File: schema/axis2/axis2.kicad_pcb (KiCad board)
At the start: 2 copper layers, 69 x 110 mm, 19 parts, among them J1 JA, J2 JB, J3 5VPower, J4 12VPower, J5 Power Motor 1, J6 Power Motor 2, J7 M1, J8 M2, J9 RC-PPM, Q1 BC547, U1 gy-9250, U2 L7805, U3 axis2-frame

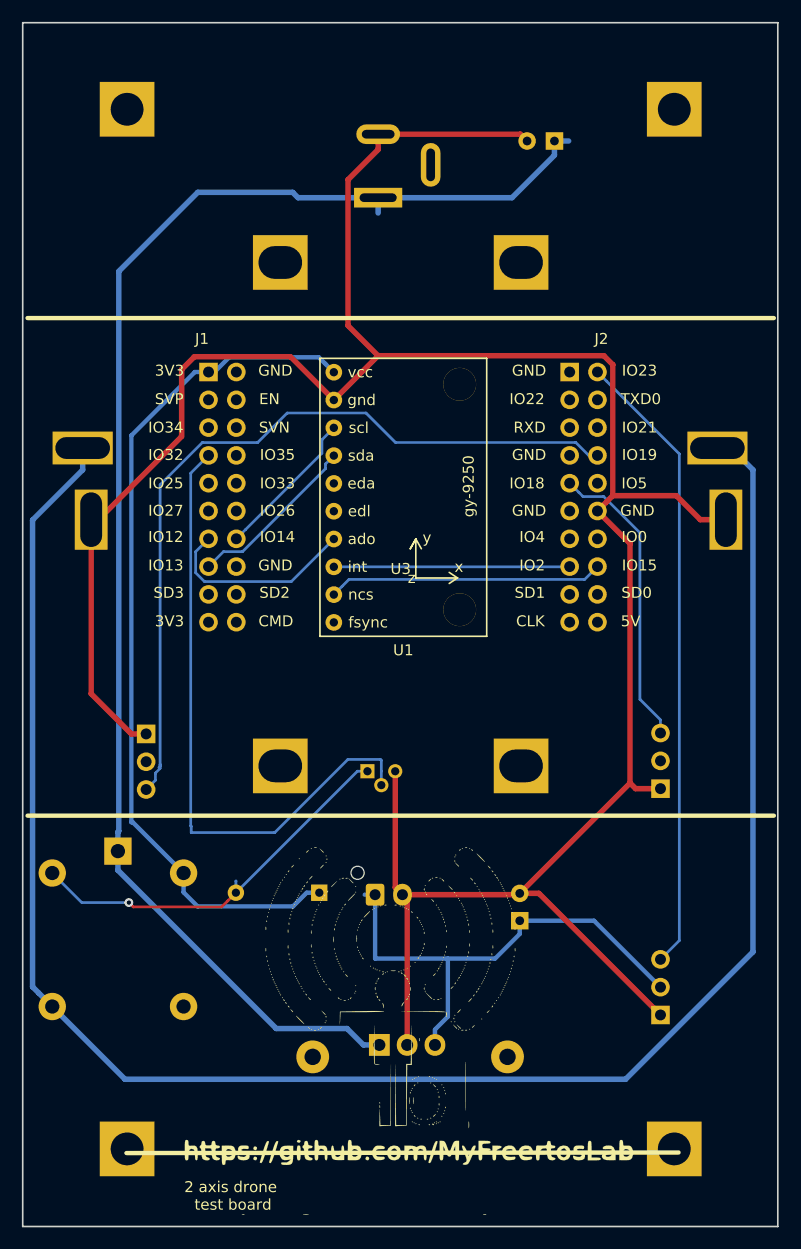
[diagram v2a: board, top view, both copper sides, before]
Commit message: Corretto scheda per errato posizionamento alimentazione esp32
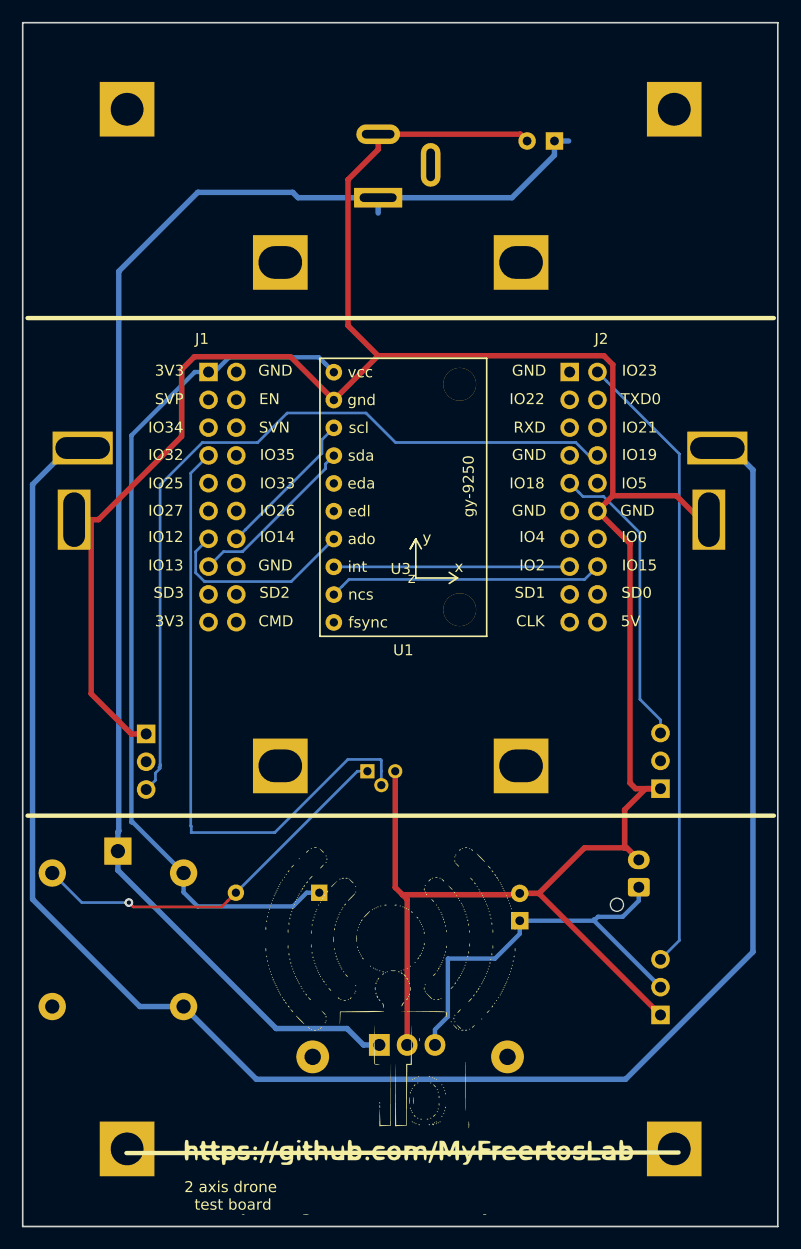
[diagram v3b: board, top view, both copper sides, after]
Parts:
- moved J3 24.1 mm to (135.3, 129.0), turned to 90 degrees
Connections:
- RLY1 pad 3: Net-(RLY1-Pad3) -> +12VM
- RLY1 pad 4: +12VM -> Net-(RLY1-Pad4)
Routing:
- net +5V: track 45.9 -> 38.7 mm
- net GND: track 243.2 -> 247.9 mm
- net +12VM: track 175.2 -> 171.2 mm
- net Net-(D1-Pad2): track 36.3 -> 35.2 mm
